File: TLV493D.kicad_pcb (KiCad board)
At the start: 2 copper layers, 14 x 22.6 mm, 18 parts, among them J1 Conn_01x04_Female, U1 TLV493D

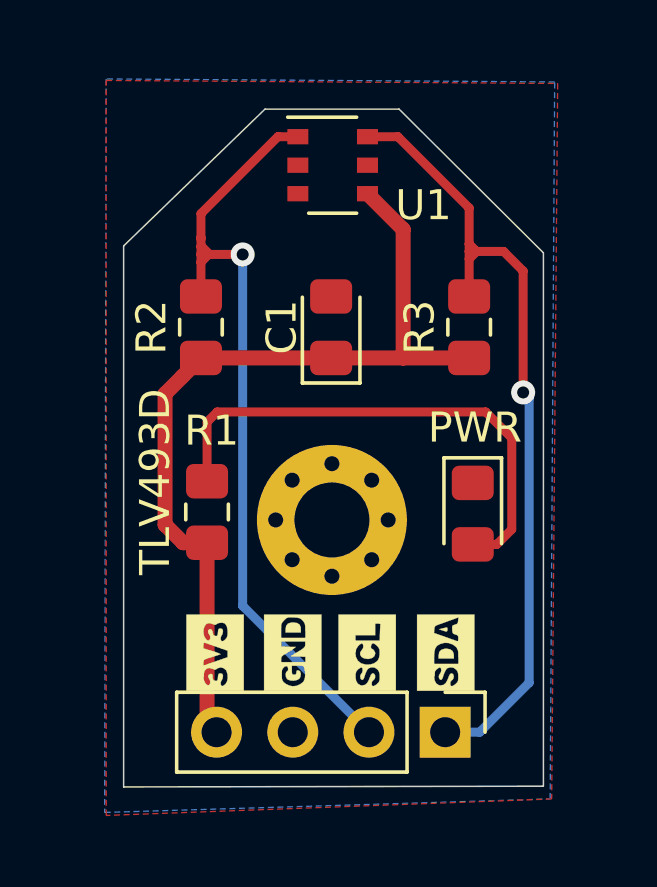
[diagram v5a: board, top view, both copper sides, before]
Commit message: plane of GND
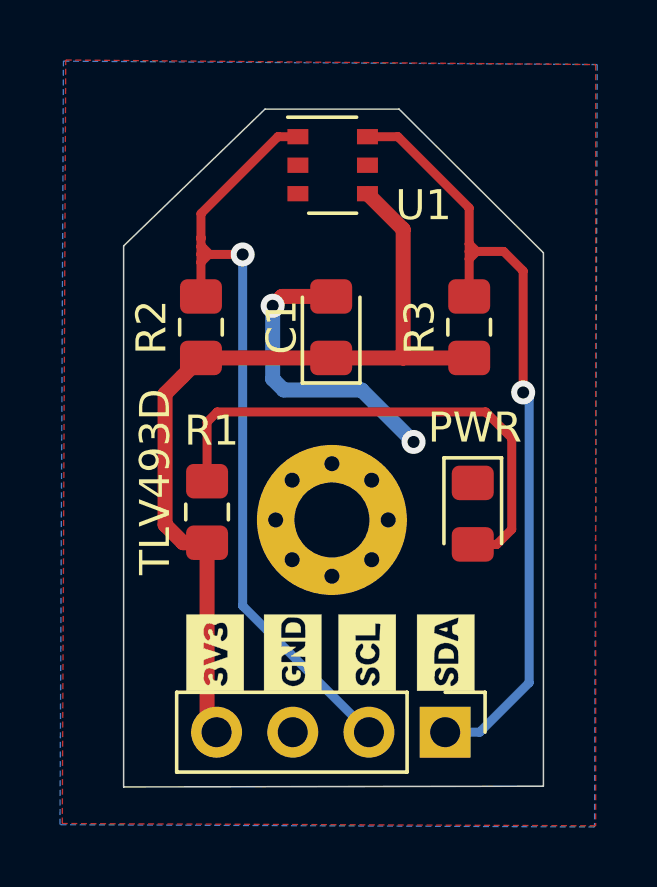
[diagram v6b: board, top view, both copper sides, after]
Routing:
- net GND: track 0.00 -> 10.1 mm, vias 0 -> 2
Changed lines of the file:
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@@
     (thickness 1.6)
     (drawings 17)
-    (tracks 55)
+    (tracks 63)
     (zones 0)
     (modules 18)
@@
   (gr_line (start 148.082 120.65) (end 162.075 120.625) (layer Edge.Cuts) (width 0.05))
   (gr_line (start 162.075 102.845) (end 162.075 120.625) (layer Edge.Cuts) (width 0.05))
+  (via (at 153.05 104.6099) (size 0.8) (drill 0.4) (layers F.Cu B.Cu) (net 1))
+  (segment (start 155 104.3) (end 153.3599 104.3) (width 0.5) (layer F.Cu) (net 1))
+  (segment (start 153.3599 104.3) (end 153.05 104.6099) (width 0.5) (layer F.Cu) (net 1))
+  (segment (start 153.05 104.6099) (end 153.05 107.0506) (width 0.5) (layer B.Cu) (net 1))
+  (segment (start 153.05 107.0506) (end 153.416 107.4166) (width 0.5) (layer B.Cu) (net 1))
+  (via (at 157.7467 109.15) (size 0.8) (drill 0.4) (layers F.Cu B.Cu) (net 1))
+  (segment (start 153.416 107.4166) (end 156.0133 107.4166) (width 0.5) (layer B.Cu) (net 1))
+  (segment (start 156.0133 107.4166) (end 157.7467 109.15) (width 0.5) (layer B.Cu) (net 1))
   (segment (start 150.8633 118.5083) (end 151.18 118.825) (width 0.5) (layer F.Cu) (net 2))
   (segment (start 150.8633 112.5093) (end 150.8633 118.5083) (width 0.5) (layer F.Cu) (net 2))
@@
   (segment (start 159.6 103.05) (end 159.6 102.8) (width 0.3) (layer F.Cu) (net 5))
   (segment (start 161.4 107.5) (end 161.4 103.45) (width 0.3) (layer F.Cu) (net 5))
+  (zone (net 1) (net_name GND) (layer B.Cu) (hatch edge 0.508)
+    (connect_pads (clearance 0.508))
+    (min_thickness 0.254)
+    (fill yes (arc_segments 32) (thermal_gap 0.508) (thermal_bridge_width 0.508))
+    (polygon
+      (pts
+        (xy 146.0754 96.4565) (xy 163.8681 96.5708) (xy 163.7792 121.9835) (xy 145.9611 121.9073)
+      )
+    )
+  )
   (zone (net 1) (net_name GND) (layer F.Cu) (hatch edge 0.508)
     (connect_pads (clearance 0.508))
@@
     (polygon
       (pts
-        (xy 147.5 97.1) (xy 162.55 97.2) (xy 162.35 121.05) (xy 147.5 121.6)
+        (xy 163.8173 121.9454) (xy 146.0373 121.8692) (xy 146.1516 96.4184) (xy 163.8173 96.5708)
       )
     )
-  )
-  (zone (net 1) (net_name GND) (layer B.Cu) (hatch edge 0.508)
-    (connect_pads (clearance 0.508))
-    (min_thickness 0.254)
-    (fill yes (arc_segments 32) (thermal_gap 0.508) (thermal_bridge_width 0.508))
-    (polygon
-      (pts
-        (xy 147.45 121.5) (xy 162.3 121.05) (xy 162.45 97.15) (xy 147.5 97.05)
-      )
-    )

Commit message: Change capacitor footprint
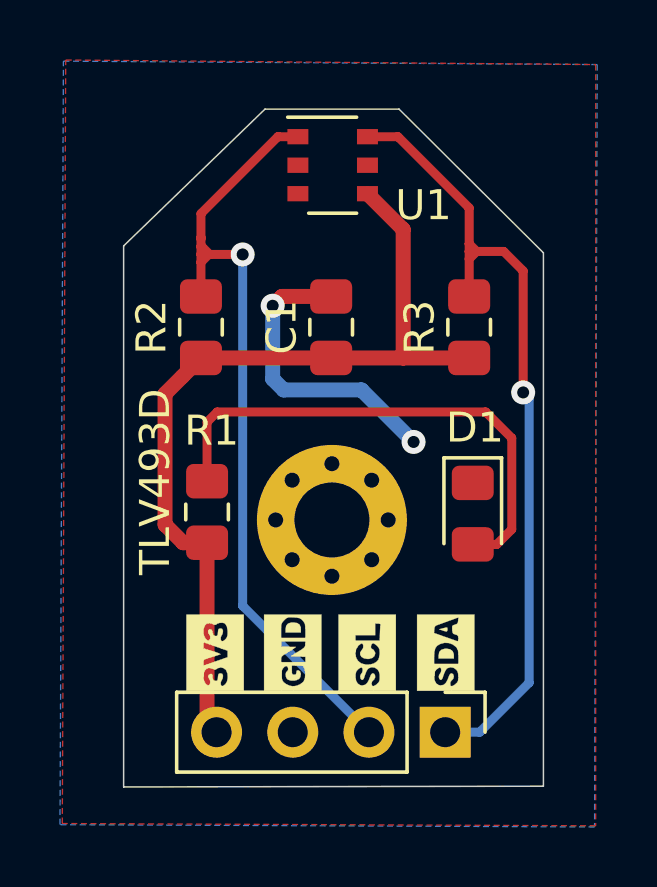
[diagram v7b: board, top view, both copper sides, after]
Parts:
- C1: footprint LED_SMD:LED_0805_2012Metric_Pad1.15x1.40mm_HandSolder -> Capacitor_SMD:C_0805_2012Metric_Pad1.15x1.40mm_HandSolder
- renumbered PWR to D1
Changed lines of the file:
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@@
-(kicad_pcb (version 20171130) (host pcbnew "(5.1.4)-1")
+(kicad_pcb (version 20171130) (host pcbnew "(5.1.0-0)")
   (general
     (thickness 1.6)
@@
     (add_net VCC)
   )
+  (module Capacitor_SMD:C_0805_2012Metric_Pad1.15x1.40mm_HandSolder (layer F.Cu)
+    (at 155 105.325 90)
+    (descr "Capacitor SMD 0805 (2012 Metric), square (rectangular) end terminal, IPC_7351 nominal with elongated pad for handsoldering. (Body size source: https://docs.google.com/spreadsheets/d/1BsfQQcO9C6DZCsRaXUlFlo91Tg2WpOkGARC1WS5S8t0/edit?usp=sharing), generated with kicad-footprint-generator")
+    (tags "capacitor handsolder")
+    (attr smd)
+    (fp_text reference C1 (at 0 -1.65 90) (layer F.SilkS)
+      (effects (font (size 1 1) (thickness 0.15)))
+    )
+    (fp_text value 0.1uF (at 0 1.65 90) (layer F.Fab)
+      (effects (font (size 1 1) (thickness 0.15)))
+    )
+    (fp_text user %R (at 0 0 90) (layer F.Fab)
+      (effects (font (size 0.5 0.5) (thickness 0.08)))
+    )
+    (fp_line (start 1.85 0.95) (end -1.85 0.95) (layer F.CrtYd) (width 0.05))
+    (fp_line (start 1.85 -0.95) (end 1.85 0.95) (layer F.CrtYd) (width 0.05))
+    (fp_line (start -1.85 -0.95) (end 1.85 -0.95) (layer F.CrtYd) (width 0.05))
+    (fp_line (start -1.85 0.95) (end -1.85 -0.95) (layer F.CrtYd) (width 0.05))
+    (fp_line (start -0.261252 0.71) (end 0.261252 0.71) (layer F.SilkS) (width 0.12))
+    (fp_line (start -0.261252 -0.71) (end 0.261252 -0.71) (layer F.SilkS) (width 0.12))
+    (fp_line (start 1 0.6) (end -1 0.6) (layer F.Fab) (width 0.1))
+    (fp_line (start 1 -0.6) (end 1 0.6) (layer F.Fab) (width 0.1))
+    (fp_line (start -1 -0.6) (end 1 -0.6) (layer F.Fab) (width 0.1))
+    (fp_line (start -1 0.6) (end -1 -0.6) (layer F.Fab) (width 0.1))
+    (pad 2 smd roundrect (at 1.025 0 90) (size 1.15 1.4) (layers F.Cu F.Paste F.Mask) (roundrect_rratio 0.217391)
+      (net 1 GND))
+    (pad 1 smd roundrect (at -1.025 0 90) (size 1.15 1.4) (layers F.Cu F.Paste F.Mask) (roundrect_rratio 0.217391)
+      (net 2 VCC))
+    (model ${KISYS3DMOD}/Capacitor_SMD.3dshapes/C_0805_2012Metric.wrl
+      (at (xyz 0 0 0))
+      (scale (xyz 1 1 1))
+      (rotate (xyz 0 0 0))
+    )
+  )
   (module Aesthetics:SCL (layer F.Cu)
     (at 156.2 116.19 90)
@@
     (tags "LED handsolder")
     (attr smd)
-    (fp_text reference PWR (at -2.8661 -0.0714 180) (layer F.SilkS)
+    (fp_text reference D1 (at -2.8661 -0.0714 180) (layer F.SilkS)
       (effects (font (size 1 1) (thickness 0.15)))
     )
@@
     (pad 1 thru_hole circle (at 0 0) (size 5 5) (drill 2.5) (layers *.Cu *.Mask))
   )
-  (module LED_SMD:LED_0805_2012Metric_Pad1.15x1.40mm_HandSolder (layer F.Cu)
-    (at 155 105.325 90)
-    (descr "LED SMD 0805 (2012 Metric), square (rectangular) end terminal, IPC_7351 nominal, (Body size source: https://docs.google.com/spreadsheets/d/1BsfQQcO9C6DZCsRaXUlFlo91Tg2WpOkGARC1WS5S8t0/edit?usp=sharing), generated with kicad-footprint-generator")
-    (tags "LED handsolder")
-    (attr smd)
-    (fp_text reference C1 (at 0 -1.65 90) (layer F.SilkS)
-      (effects (font (size 1 1) (thickness 0.15)))
-    )
-    (fp_text value 0.1uF (at 0 1.65 90) (layer F.Fab)
-      (effects (font (size 1 1) (thickness 0.15)))
-    )
-    (fp_line (start 1 -0.6) (end -0.7 -0.6) (layer F.Fab) (width 0.1))
-    (fp_line (start -0.7 -0.6) (end -1 -0.3) (layer F.Fab) (width 0.1))
-    (fp_line (start -1 -0.3) (end -1 0.6) (layer F.Fab) (width 0.1))
-    (fp_line (start -1 0.6) (end 1 0.6) (layer F.Fab) (width 0.1))
-    (fp_line (start 1 0.6) (end 1 -0.6) (layer F.Fab) (width 0.1))
-    (fp_line (start 1 -0.96) (end -1.86 -0.96) (layer F.SilkS) (width 0.12))
-    (fp_line (start -1.86 -0.96) (end -1.86 0.96) (layer F.SilkS) (width 0.12))
-    (fp_line (start -1.86 0.96) (end 1 0.96) (layer F.SilkS) (width 0.12))
-    (fp_line (start -1.85 0.95) (end -1.85 -0.95) (layer F.CrtYd) (width 0.05))
-    (fp_line (start -1.85 -0.95) (end 1.85 -0.95) (layer F.CrtYd) (width 0.05))
-    (fp_line (start 1.85 -0.95) (end 1.85 0.95) (layer F.CrtYd) (width 0.05))
-    (fp_line (start 1.85 0.95) (end -1.85 0.95) (layer F.CrtYd) (width 0.05))
-    (fp_text user %R (at 0 0 90) (layer F.Fab)
-      (effects (font (size 0.5 0.5) (thickness 0.08)))
-    )
-    (pad 1 smd roundrect (at -1.025 0 90) (size 1.15 1.4) (layers F.Cu F.Paste F.Mask) (roundrect_rratio 0.217391)
-      (net 2 VCC))
-    (pad 2 smd roundrect (at 1.025 0 90) (size 1.15 1.4) (layers F.Cu F.Paste F.Mask) (roundrect_rratio 0.217391)
-      (net 1 GND))
-    (model ${KISYS3DMOD}/LED_SMD.3dshapes/LED_0805_2012Metric.wrl
-      (at (xyz 0 0 0))
-      (scale (xyz 1 1 1))
-      (rotate (xyz 0 0 0))
-    )
-  )
   (module Connector_PinHeader_2.54mm:PinHeader_1x04_P2.54mm_Vertical (layer F.Cu)
